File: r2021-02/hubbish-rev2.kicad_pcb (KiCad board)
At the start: 4 copper layers, 100 x 80 mm, 124 parts, among them J1 Conn_01x06, J2 USB_A_Stacked, J3 USB_A_Stacked, J4 USB_A (female down), J5 Conn_01x03_Male, J6 USB_A_Stacked, J8 USB_A male UP, J9 USB_B_Micro (up), Q1 Si4435, U1 2k i2c eeprom, U10 NUP4202, U11 NUP4202, U12 NUP4202, U13 NUP4202, U14 NUP4202, U15 NUP4202, U16 NUP4202, U17 NUP4202, U18 SE5120ST33, U19 APL3511C, U2 SiC437AED, U3 USB2517, U4 APL3511C, U5 APL3511C, U6 APL3511C, U7 APL3511C, U8 APL3511C, U9 APL3511C, Y1 24MHz

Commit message: r2: start really doing some power routing...
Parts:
- removed NT1: NetTie_2, NetTie:NetTie-2_SMD_Pad0.5mm
- moved C42 34.8 mm to (97.2, 99.5), turned to -90 degrees
- moved C45 29.9 mm to (95.0, 99.5), turned to -90 degrees
- moved C40 26.5 mm to (92.8, 93.9), turned to 180 degrees
- moved C41 26.3 mm to (92.8, 87.4), turned to 180 degrees
- moved R23 8.26 mm to (121.8, 81.6)
- moved D1 7.66 mm to (111.2, 81.2)
- moved Q1 7.39 mm to (117.5, 83.8)
- moved D13 7.26 mm to (102.0, 80.5)
- moved J1 6.90 mm to (120.0, 77.0)
- moved D12 4.73 mm to (121.8, 85.7), turned to 90 degrees
- moved R29 3.84 mm to (114.0, 97.2), turned to -90 degrees
- moved C37 3.82 mm to (107.8, 98.7)
- moved C38 3.79 mm to (114.2, 91.2)
- moved R28 3.71 mm to (114.2, 92.8)
- moved C31 3.68 mm to (109.6, 88.2)
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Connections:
- C34 pad 2: GNDA -> GND
- C36 pad 2: GNDA -> GND
- R25 pad 1: GNDA -> GND
- R27 pad 1: GNDA -> GND
- R30 pad 2: GNDA -> GND
- U2 pad 16: GNDA -> GND
- U2 pad 25: GNDA -> GND
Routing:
- net /power_input/MODE2: track 0.00 -> 11.1 mm, vias 0 -> 2
- net /power_input/MODE1: track 0.00 -> 10.5 mm, vias 0 -> 2
- net +VDC: track 0.00 -> 9.49 mm, vias 0 -> 1
- net /power_input/PolProtG: track 0.00 -> 4.96 mm
- net /power_input/fb: track 0.00 -> 4.45 mm
- net +5V: track 50.7 -> 53.7 mm, vias 8 -> 25
- net /power_input/VDRV: track 0.00 -> 2.57 mm
- net /power_input/VDD: track 0.00 -> 2.48 mm
- net /power_input/phase: track 0.00 -> 2.34 mm
- net /power_input/boot: track 0.00 -> 1.85 mm
- net Net-(C38-Pad1): track 0.00 -> 1.54 mm
- net GND: track 134.5 -> 135.7 mm, vias 38 -> 42
- added copper zone on F.Cu, net +5V
- added copper zone on F.Cu, net +VDC
- added copper zone on F.Cu, net /power_input/PWR_RAW
- added copper zone on F.Cu, net /power_input/SW

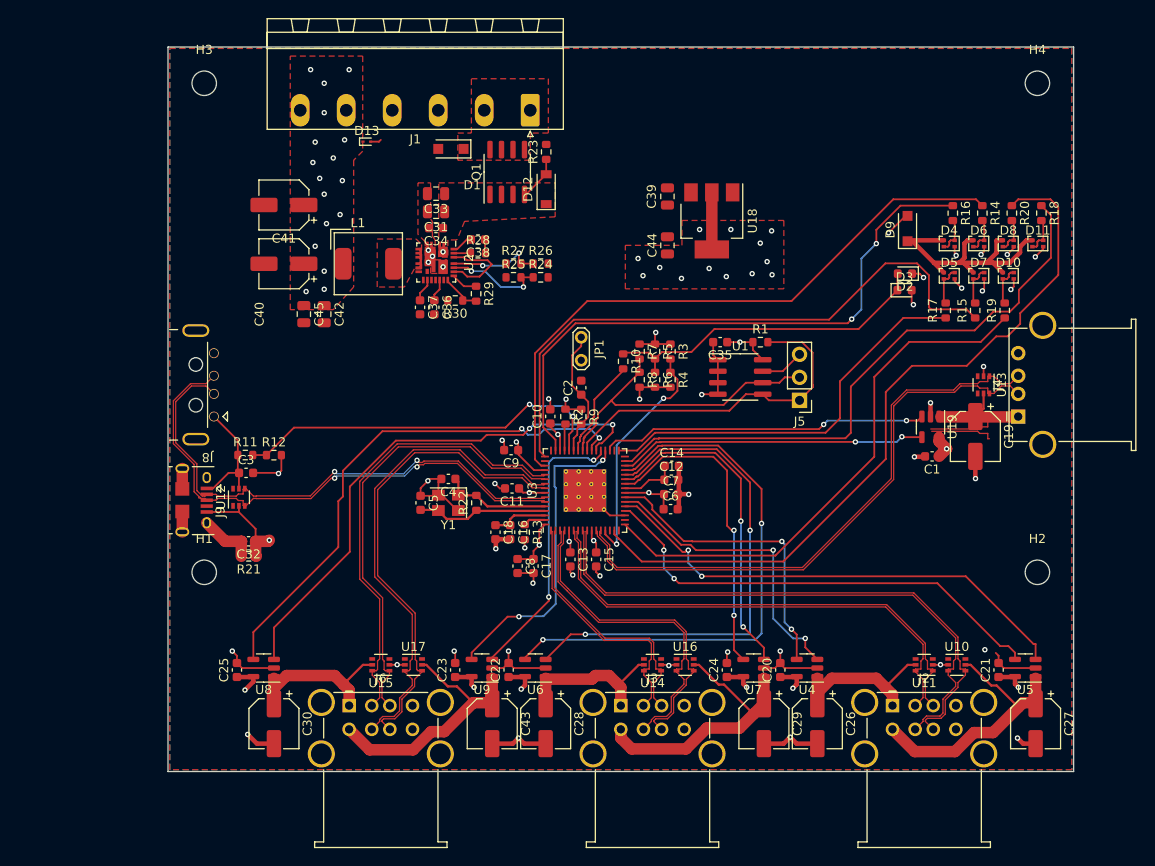
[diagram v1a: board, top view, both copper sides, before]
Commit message: "finished" rev2?
ok, should we go and order this damn thing?  try it one more time?

M2.5, should i use m3?
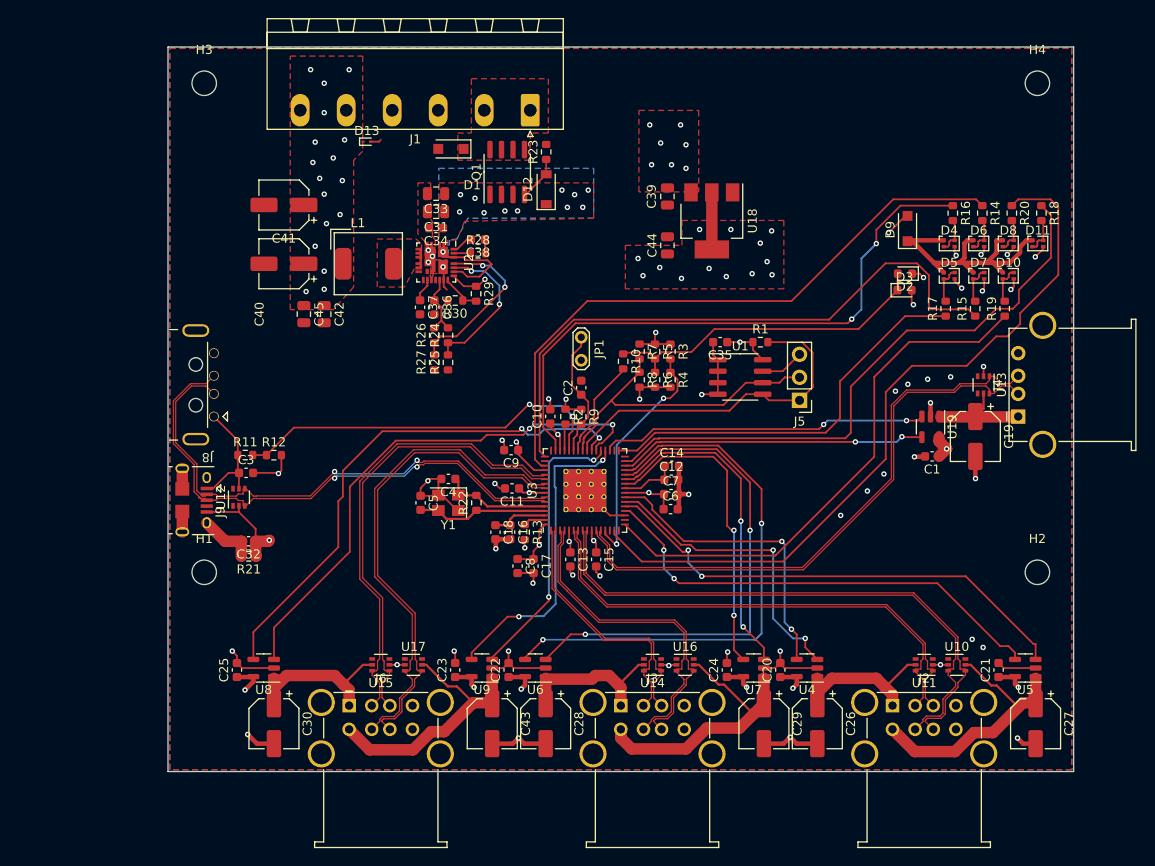
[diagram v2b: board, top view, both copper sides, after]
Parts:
- moved R26 14.2 mm to (109.4, 101.8), turned to 90 degrees
- moved R27 14.0 mm to (109.4, 104.8), turned to 90 degrees
- moved R24 12.1 mm to (110.9, 101.8), turned to 90 degrees
- moved R25 11.9 mm to (110.9, 104.8), turned to 90 degrees
- moved R15 0.20 mm to (169.1, 98.9)
- moved R17 0.20 mm to (165.9, 98.9)
- moved R19 0.20 mm to (172.4, 98.9)
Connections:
- U2 pad 10: (no net) -> unconnected-(U2-Pad10)
- U2 pad 11: unconnected-(U2-Pad11) -> unconnected-(U2-Pad10)
- U2 pad 28: (no net) -> unconnected-(U2-Pad10)
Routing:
- net /power_input/MODE1: track 10.5 -> 18.9 mm
- net /downstream-port-power/VBUS_DS: track 18.6 -> 11.5 mm
- net /power_input/MODE2: track 11.1 -> 16.9 mm
- net +5V: track 53.7 -> 47.9 mm, vias 25 -> 32
- net /power_input/VDD: track 2.48 -> 7.25 mm
- net GND: track 135.7 -> 137.3 mm, vias 42 -> 51
- net +VDC: track 9.49 -> 10.3 mm, vias 1 -> 12
- added copper zone on B.Cu, net +VDC

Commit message: overhaul, push silk, complete "again"
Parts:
- added TP1: TestPoint, et-parts:TestPoint_Plated_Hole_0.6_D0.8mm, F.Cu at (98.9, 82.3)
- added TP2: TestPoint, et-parts:TestPoint_Plated_Hole_0.6_D0.8mm, F.Cu at (107.2, 109.7)
- added TP3: TestPoint, et-parts:TestPoint_Plated_Hole_0.6_D0.8mm, F.Cu at (83.6, 95.4)
- moved C41 44.3 mm to (97.8, 110.2), turned to 0 degrees
- moved U19 42.7 mm to (100.5, 105.3), turned to 0 degrees
- moved C44 36.9 mm to (103.2, 110.2), turned to 180 degrees
- moved C4 7.70 mm to (111.5, 127.2), turned to 0 degrees
- moved R19 6.99 mm to (172.9, 98.9)
- moved C5 6.75 mm to (108.8, 124.1), turned to -90 degrees
- moved R22 6.69 mm to (166.5, 88.0)
- moved D5 6.60 mm to (172.9, 95.3)
- moved D4 6.60 mm to (172.9, 91.7)
- moved D9 6.29 mm to (166.5, 95.3)
- moved D8 6.28 mm to (166.5, 91.7)
- moved R18 6.21 mm to (172.9, 88.0)
- moved R21 5.89 mm to (166.5, 98.9)
- moved Y1 3.79 mm to (111.5, 124.1), turned to -90 degrees
- moved R12 3.24 mm to (114.0, 123.6)
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- renumbered C35 to C1, C9 to C10, C10 to C11, C11 to C12, C12 to C13, C13 to C14, C14 to C15, C15 to C16, C16 to C17, C17 to C18, C18 to C19, C32 to C2, C1 to C26, C19 to C27, C26 to C28, C27 to C29, C2 to C3, C28 to C30, C29 to C31, C30 to C32, C43 to C33, C31 to C34, C33 to C35, C34 to C36, C36 to C37, C37 to C38, C38 to C39, C5 to C4, C39 to C41, C41 to C42, C42 to C43, C4 to C5, C3 to C6, C6 to C7, C7 to C8, C8 to C9, D3 to D1, D11 to D10, D1 to D11, D9 to D3, D10 to D9, J5 to J1, J8 to J2, J9 to J3, J2 to J5, J3 to J6, J6 to J7, J1 to J8, R21 to R1, R2 to R11, R22 to R12, R11 to R13, R12 to R14, R13 to R15, R14 to R16, R15 to R17, R16 to R18, R17 to R19, R1 to R2, R18 to R20, R19 to R21, R20 to R22, U19 to U10, U13 to U11, U11 to U12, U14 to U13, U15 to U14, U10 to U15, U2 to U18, U18 to U19, U12 to U2
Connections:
- net /upstream-config-leds/LA_6-6 renamed /upstream-config-leds/LA_7-6
- net /upstream-config-leds/LA_7-5 renamed /upstream-config-leds/LA_6-5
- R21 pad 1: /upstream-config-leds/LED_A6 -> /upstream-config-leds/LED_A7
- R22 pad 1: /upstream-config-leds/LED_A7 -> /upstream-config-leds/LED_A6
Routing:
- net /upstream-config-leds/LED_A7: track 82.1 -> 56.1 mm, vias 0 -> 2
- net /upstream-config-leds/LED_A3: track 67.3 -> 75.9 mm
- net /upstream-config-leds/LED_A6: track 59.5 -> 66.7 mm, vias 0 -> 2
- net /upstream-config-leds/LED_A4: track 44.6 -> 51.6 mm
- net +5V: track 47.9 -> 54.1 mm, vias 32 -> 28
- net /downstream-port-power/U6-: track 54.1 -> 48.4 mm
- net /downstream-port-power/U6+: track 53.5 -> 48.0 mm
- net /downstream-port-power/EN2: track 51.8 -> 56.6 mm
- net /upstream-config-leds/LED_A5: track 66.4 -> 70.4 mm
- net /upstream-config-leds/xtal2: track 12.1 -> 15.8 mm
- net /upstream-config-leds/UP-: track 59.7 -> 56.5 mm
- net /downstream-port-power/OC2: track 54.3 -> 57.4 mm
- net /upstream-config-leds/LED_DRIVE: track 31.9 -> 28.9 mm
- net /downstream-port-power/EN3: track 61.6 -> 64.5 mm
- net /upstream-config-leds/UP+: track 60.3 -> 57.4 mm
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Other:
- board text added: "3V3"
- board text added: "5(6) 3(1) 1(3) DS(5) 6(7) 4(2) 2(4)"
- board text added: "5V"
- board text added: "5V 5V GND GND IN+ IN+"
- board text added: "CFG0 CFG1 CFG2"
- board text added: "DS(5)"
- board text added: "Downstream ==>>"
- board text added: "EEPROM GND SCL SDA"
- board text added: "GND"
- board text added: "Green Red Orange"
- board text added: "HUBBISH r2"
- board text added: "Hi Lo"
- board text added: "Hubbish r2 2022-06 false.ekta.is"
- board text added: "LS FS HS"
- board text added: "M1 M2"
- board text added: "Port Speeds"
- board text added: "RESET"
- board text added: "U1(3) U2(4)"
- board text added: "U3(1) U4(2)"
- board text added: "U5(6) U6(7)"
- board text added: "USB2-HS, 7 Port, Cascadeable 7x1Amp supply per port power switching Optional EEPROM"
- board text added: "Upstream <<=="
- board text added: "Vin: 6-30V P: 30W"

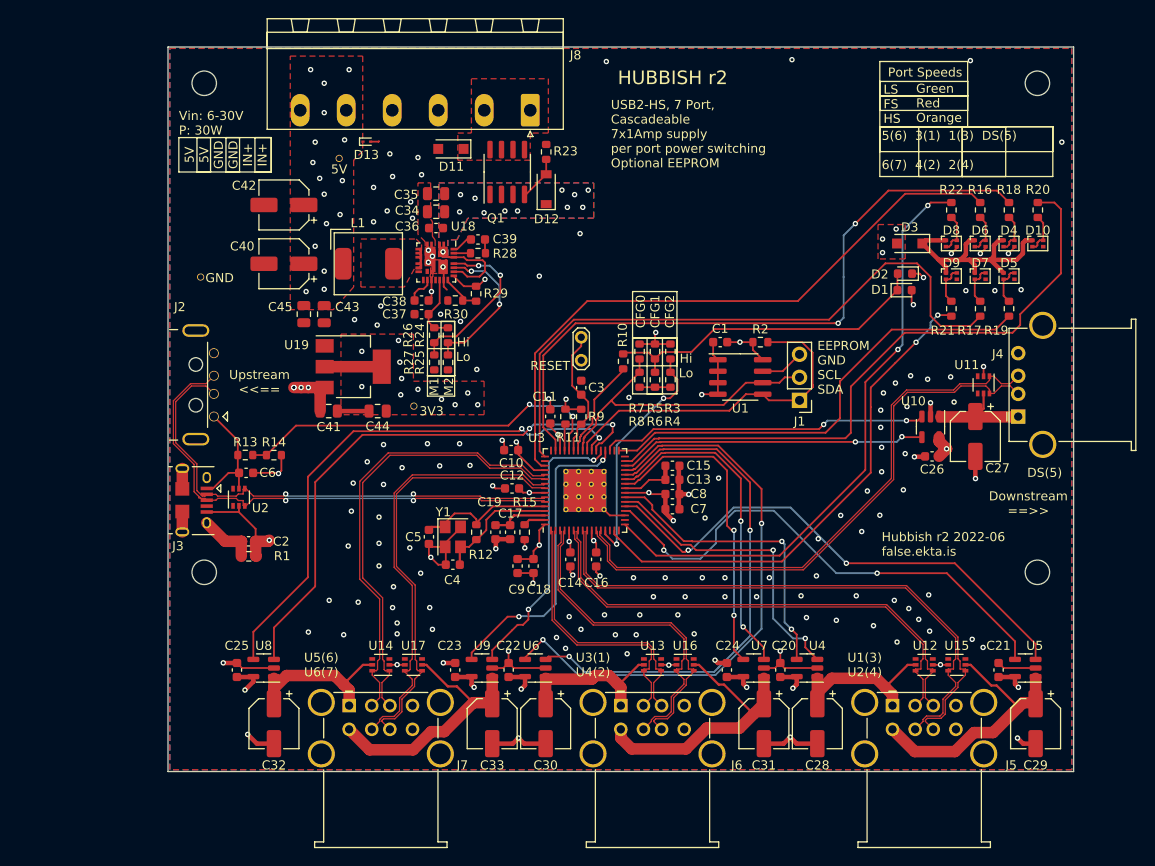
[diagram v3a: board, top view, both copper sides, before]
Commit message: r2: push more, switch to m3 mounting, more silk
added a chicken jumper to connect vbus and 5v...
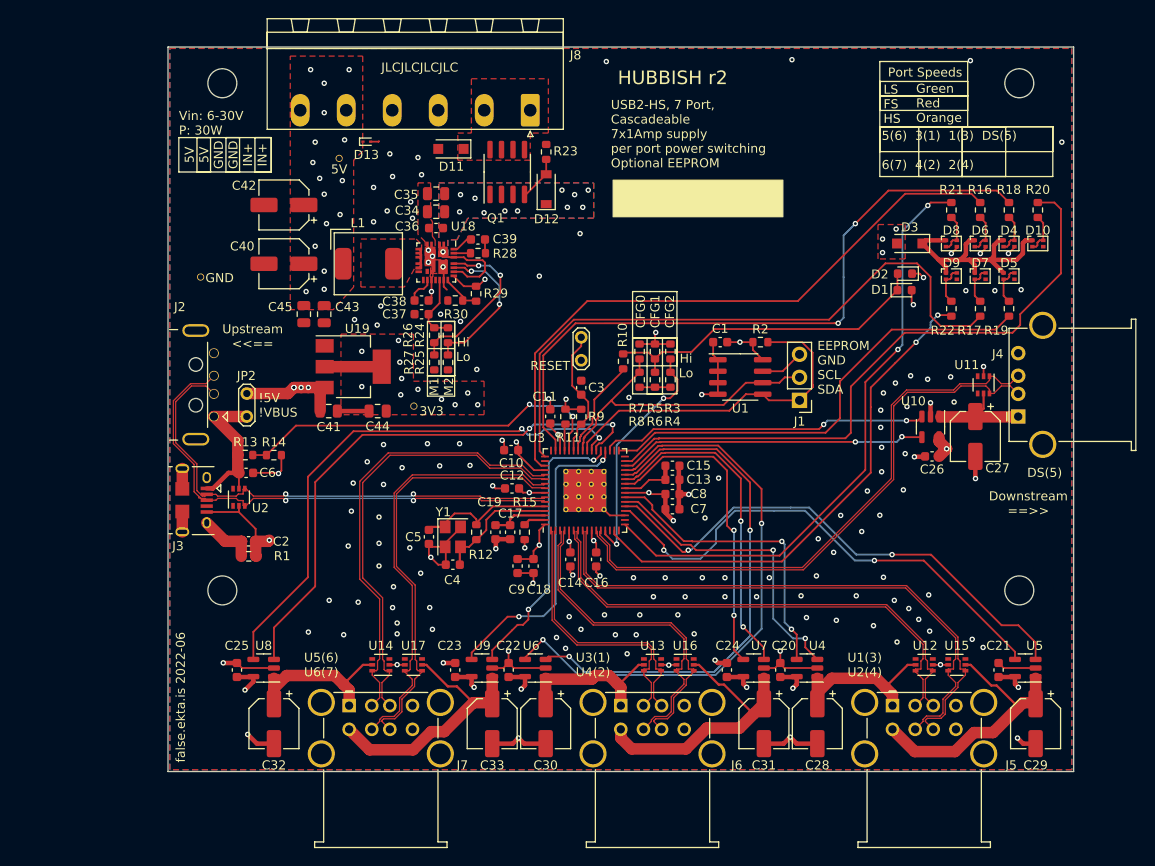
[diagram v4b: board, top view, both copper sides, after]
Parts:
- added JP2: Jumper_2_Open, TestPoint:TestPoint_2Pads_Pitch2.54mm_Drill0.8mm, F.Cu at (88.7, 110.8)
- H1, H2, H3, H4: footprint MountingHole:MountingHole_2.7mm_M2.5 -> MountingHole:MountingHole_3.2mm_M3
- moved H1 2.83 mm to (86.0, 130.0)
- moved H2 2.83 mm to (174.0, 130.0)
- moved H3 2.00 mm to (86.0, 74.0)
- moved H4 2.00 mm to (174.0, 74.0)
- renumbered R22 to R21, R21 to R22
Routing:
- net +5V: track 54.1 -> 59.6 mm
- net /upstream-config-leds/VBUS_UP: track 13.4 -> 17.0 mm
- net /downstream-port-power/EN2: track 56.6 -> 56.0 mm
- net GND: vias 143 -> 145
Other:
- board text added: "!5V !VBUS"
- board text added: "JLCJLCJLCJLC"
- board text added: "false.ekta.is 2022-06"
- board text removed: "Hubbish r2 2022-06 false.ekta.is"
